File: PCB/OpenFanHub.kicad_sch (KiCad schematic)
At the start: 99 parts, among them J1 Conn_ARM_JTAG_SWD_10, J2 USB, J3 Conn_01x04, J4 USART1, M1 Fan_4pin, M10 Fan_4pin, M11 Fan_4pin, M12 Fan_4pin, M2 Fan_4pin, M3 Fan_4pin, M4 Fan_4pin, M5 Fan_4pin, M6 Fan_4pin, M7 Fan_4pin, M8 Fan_4pin, M9 Fan_4pin, U1 STM32F072CBTx, U2 XC6206P332MR, U3 MAX31790ATI_T, U4 MAX31790ATI_T, U5 USBLC6-2SC6, Y1 8MHz

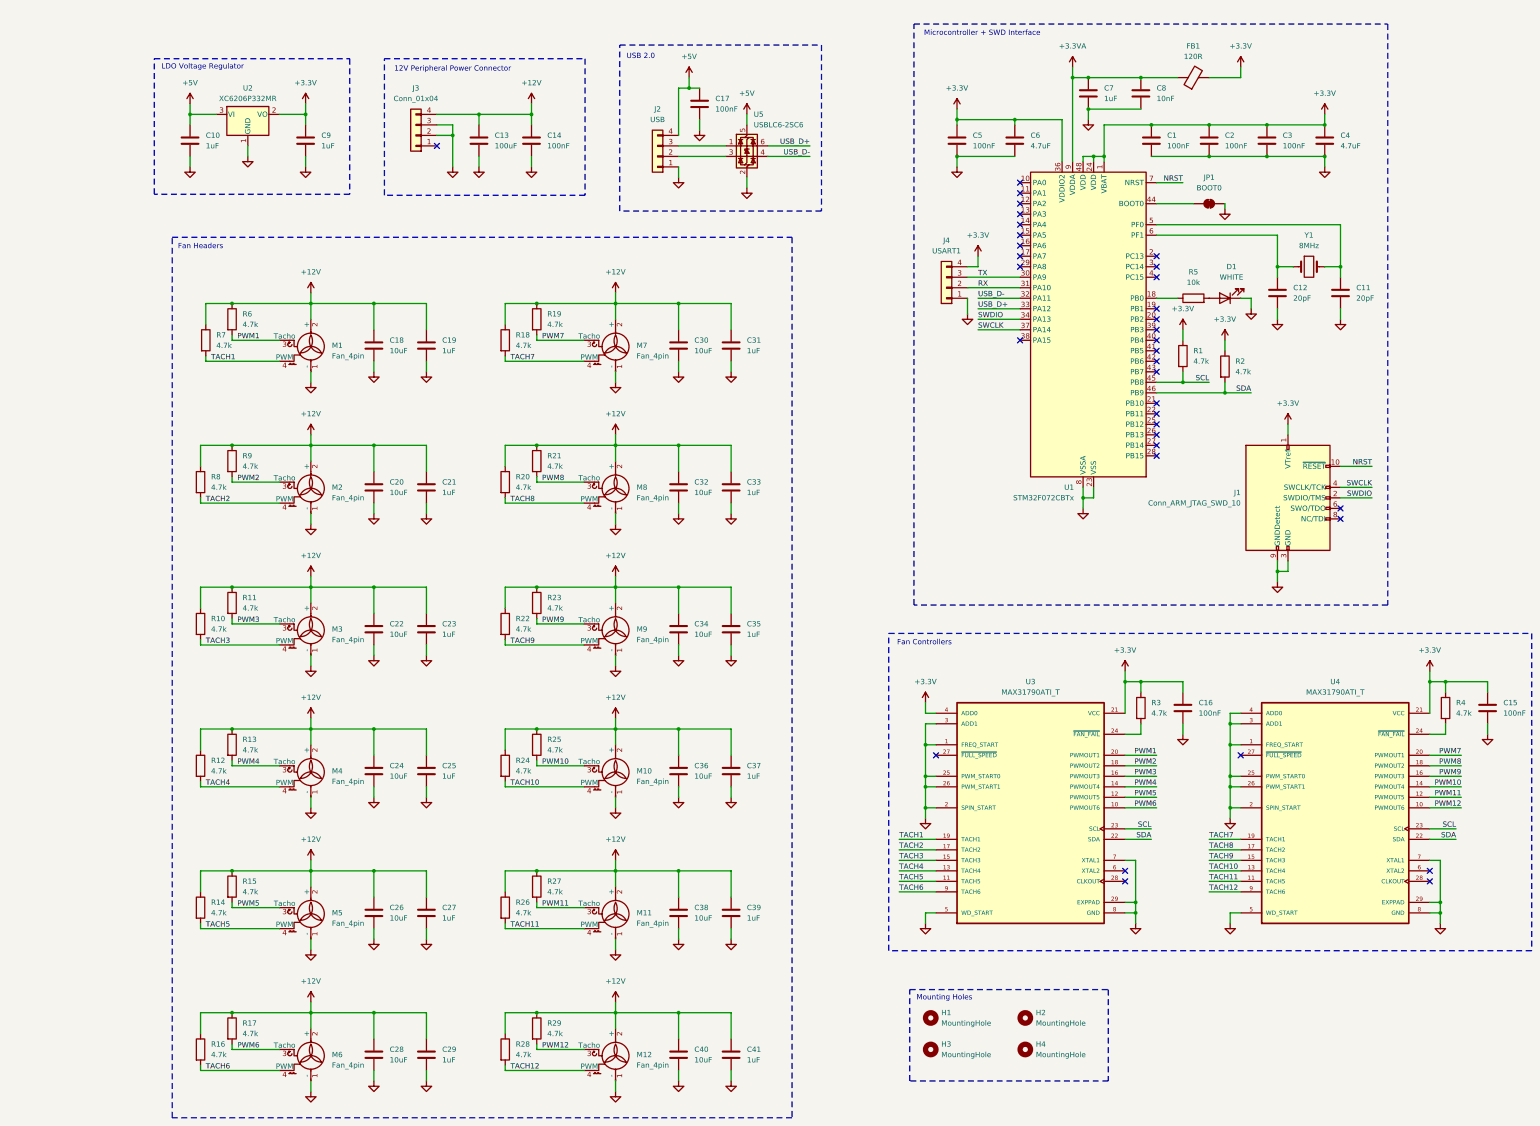
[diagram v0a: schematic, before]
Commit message: Update PCB schematic. Removed unneeded bypass capacitors on fan headers. Remove BOOT0 jumper. Remove 3V3 pin from UART pins
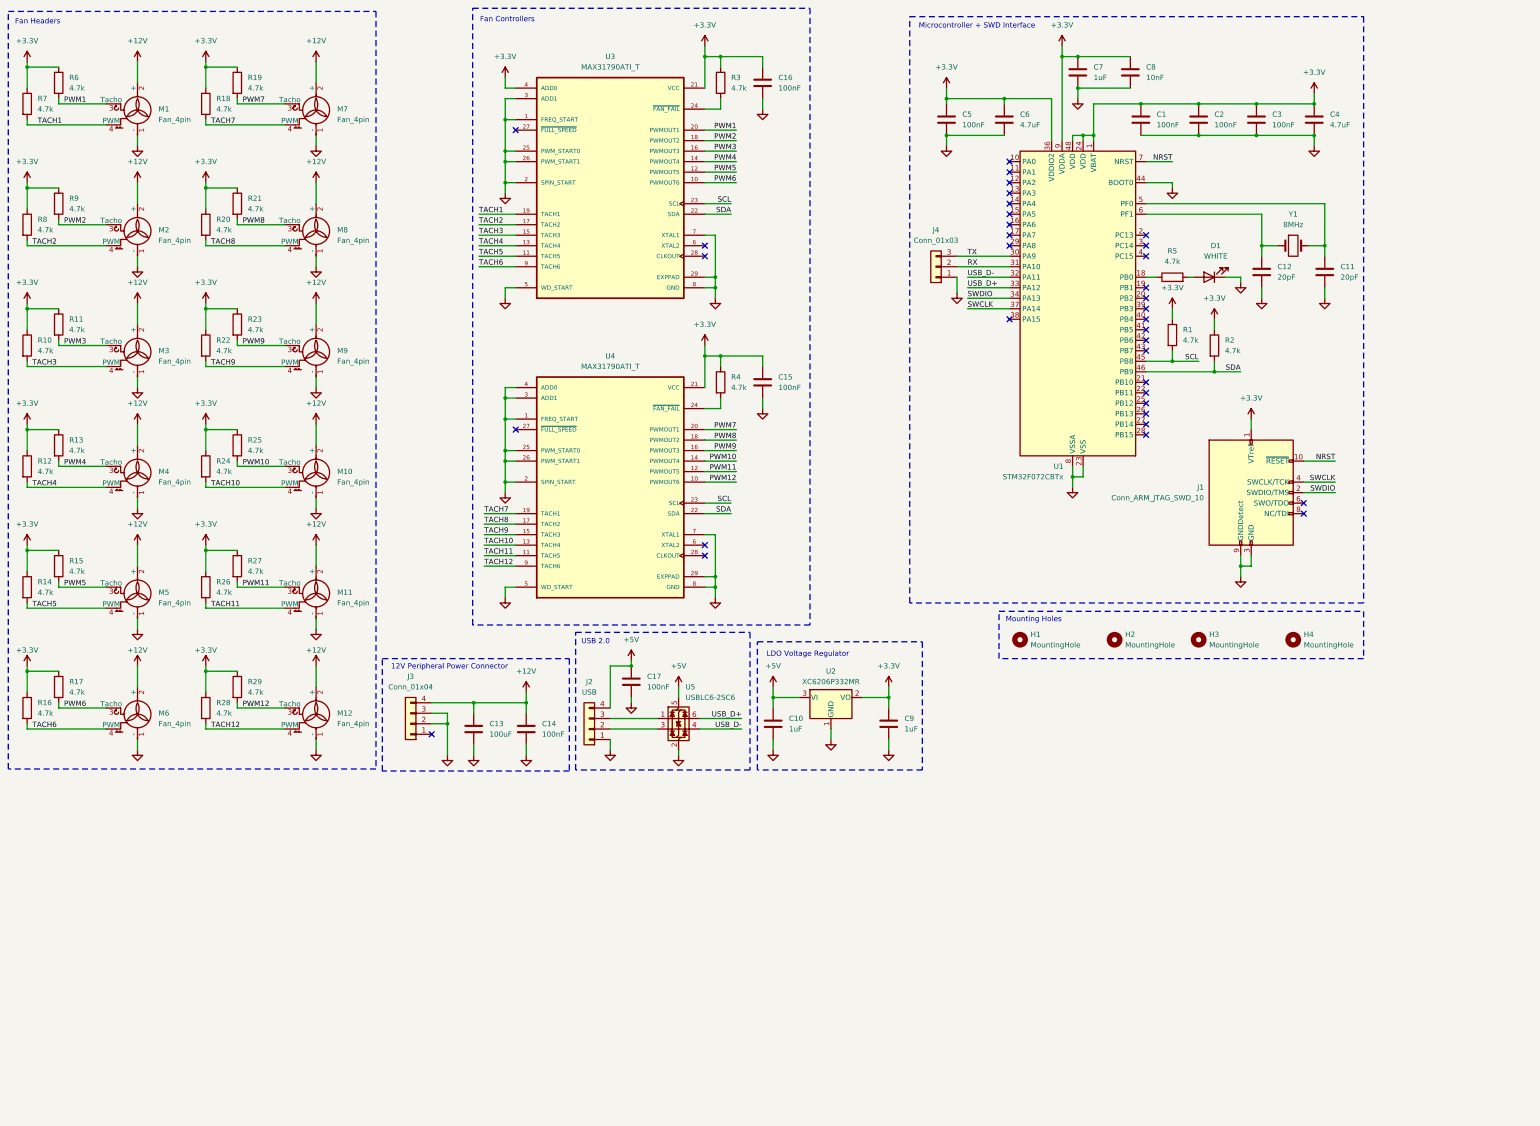
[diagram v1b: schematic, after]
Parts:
- removed C18, C20, C22, C24, C26, C28, C30, C32, C34, C36, C38, C40: 10uF, Capacitor_SMD:C_0805_2012Metric, symbol Device:C
- removed C19, C21, C23, C25, C27, C29, C31, C33, C35, C37, C39, C41: 1uF, Capacitor_SMD:C_0603_1608Metric, symbol Device:C
- removed FB1: 120R, Inductor_SMD:L_Walsin_WLFM201209x, symbol Device:FerriteBead
- removed J4: USART1, Connector_PinHeader_2.54mm:PinHeader_1x04_P2.54mm_Vertical_SMD_Pin1Left, symbol Connector_Generic:Conn_01x04
- removed JP1: BOOT0, Jumper:SolderJumper-2_P1.3mm_Bridged2Bar_Pad1.0x1.5mm, symbol Jumper:SolderJumper_2_Bridged
- added J4: Conn_01x03, Connector_PinSocket_2.54mm:PinSocket_1x03_P2.54mm_Vertical_SMD_Pin1Left, symbol Connector_Generic:Conn_01x03
- R5: value 10k -> 4.7k
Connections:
- net +3.3VA is gone; now on net +3.3V: C7.1, C8.1, U1.9 (VDDA)
- net +12V: no longer R10.1, R11.1, R12.1, R13.1, R14.1, R15.1, R16.1, R17.1, R18.1, R19.1, R20.1, R21.1, R22.1, R23.1, R24.1, R25.1, R26.1, R27.1, R28.1, R29.1, R6.1, R7.1, R8.1, R9.1
- net +3.3V: now also R10.1, R11.1, R12.1, R13.1, R14.1, R15.1, R16.1, R17.1, R18.1, R19.1, R20.1, R21.1, R22.1, R23.1, R24.1, R25.1, R26.1, R27.1, R28.1, R29.1, R6.1, R7.1, R8.1, R9.1
- net GND: now also U1.44 (BOOT0), J4.1 (Pin_1)
- net RX: now also J4.2 (Pin_2)
- net TX: now also J4.3 (Pin_3)
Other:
- moved on the sheet: C1, C10, C11, C12, C13, C14, C15, C16, C17, C2, C3, C4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
